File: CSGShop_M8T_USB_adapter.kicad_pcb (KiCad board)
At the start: 2 copper layers, 36.8 x 16.5 mm, 6 parts, among them J1 NEO-M8T Conn_02x06_Odd_Even, J2 Conn_01x05, J3 Conn_01x06_Male, J4 Conn_01x06_Male

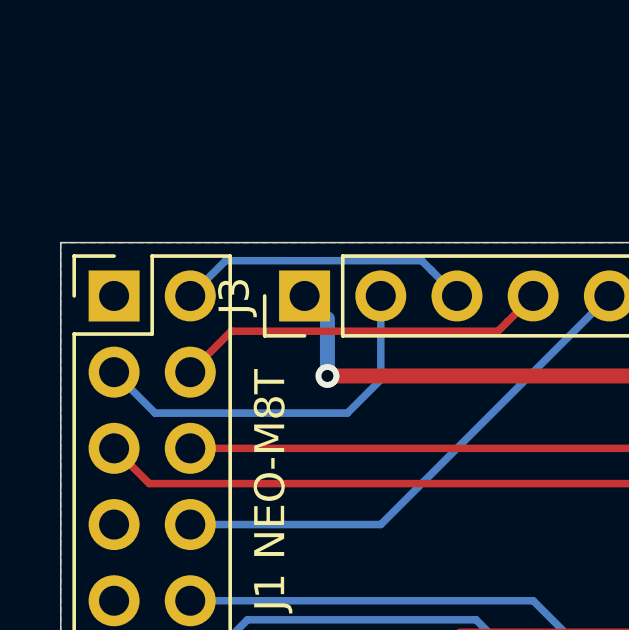
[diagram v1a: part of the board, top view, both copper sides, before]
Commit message: fix missing trace to GND on M8T header
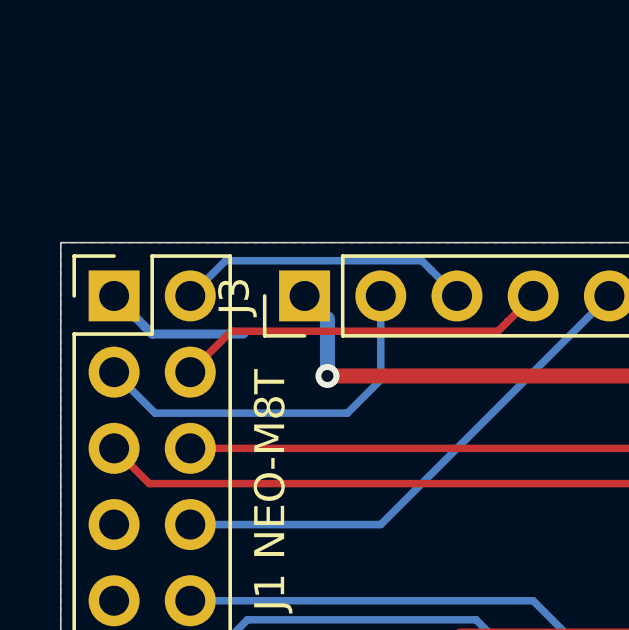
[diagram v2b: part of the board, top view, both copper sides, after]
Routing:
- net GND: track 55.3 -> 60.1 mm
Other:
- board text added: "CSGShop M8T (pin version) USB adapter V1.0.1"
- board text removed: "CSGShop M8T (pin version) USB adapter V1.0"
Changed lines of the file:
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@@
-(kicad_pcb (version 20171130) (host pcbnew 6.0.0-rc1-unknown-4d73cfb~66~ubuntu18.04.1)
+(kicad_pcb (version 20171130) (host pcbnew 6.0.0-rc1-unknown-ad07b4a~66~ubuntu18.04.1)
   (general
     (thickness 1.6)
     (drawings 12)
-    (tracks 46)
+    (tracks 49)
     (zones 0)
     (modules 6)
@@
   )
   (setup
-    (last_trace_width 0.25)
+    (last_trace_width 0.3)
+    (user_trace_width 0.3)
     (trace_clearance 0.2)
     (zone_clearance 0.508)
@@
     (effects (font (size 1 1) (thickness 0.15)) (justify mirror))
   )
-  (gr_text "CSGShop M8T \n(pin version) \nUSB adapter V1.0" (at 137.414 53.213) (layer B.SilkS)
+  (gr_text "CSGShop M8T \n(pin version) \nUSB adapter V1.0.1" (at 137.414 53.213) (layer B.SilkS)
     (effects (font (size 1 1) (thickness 0.15)) (justify mirror))
   )
@@
   (segment (start 132.08 48.26) (end 131.318 47.498) (width 0.25) (layer B.Cu) (net 1))
   (segment (start 132.08 50.165) (end 132.08 48.26) (width 0.5) (layer B.Cu) (net 1))
+  (segment (start 124.968 47.498) (end 125.984 48.514) (width 0.3) (layer B.Cu) (net 1))
+  (segment (start 125.984 48.514) (end 126.238 48.768) (width 0.3) (layer B.Cu) (net 1))
+  (segment (start 126.238 48.768) (end 129.286 48.768) (width 0.3) (layer B.Cu) (net 1))
   (segment (start 148.375001 56.046001) (end 149.225 56.896) (width 0.25) (layer F.Cu) (net 2))
   (segment (start 146.082001 53.753001) (end 148.375001 56.046001) (width 0.25) (layer F.Cu) (net 2))

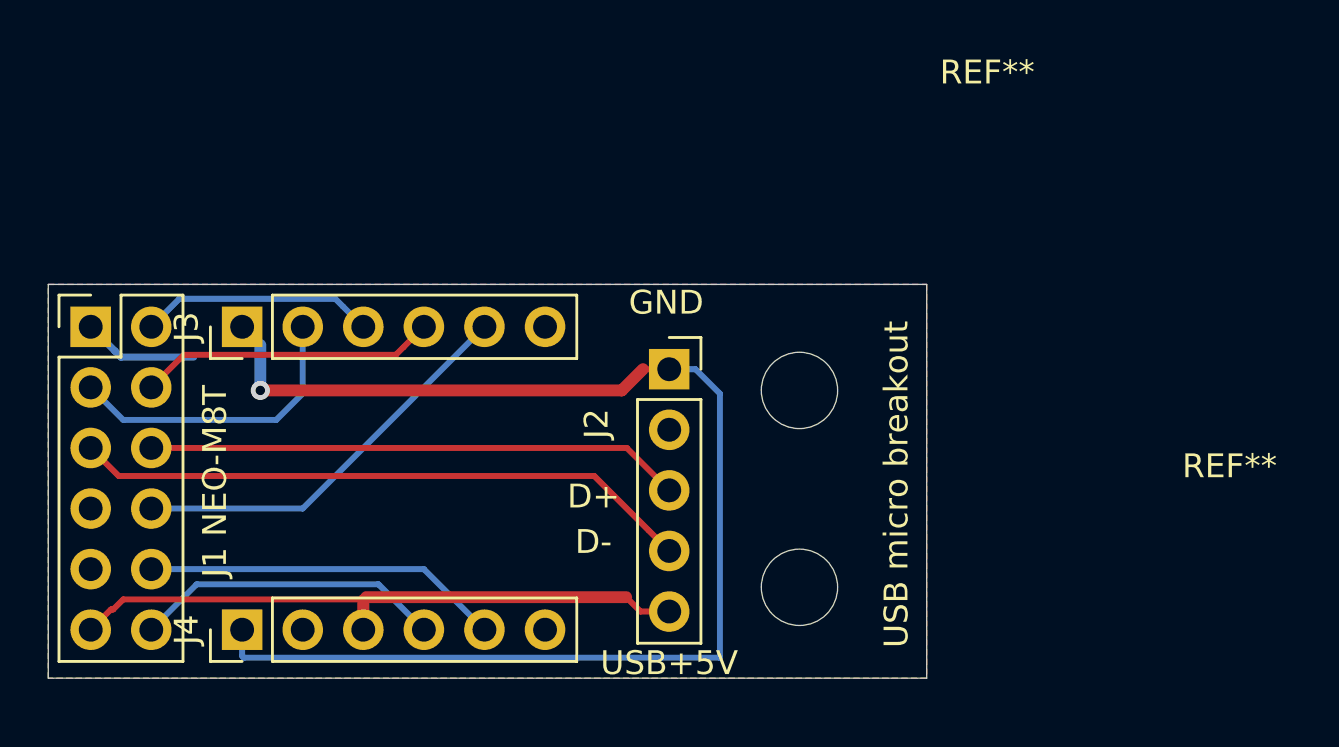
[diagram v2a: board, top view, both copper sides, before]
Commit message: add extra info on silk screen
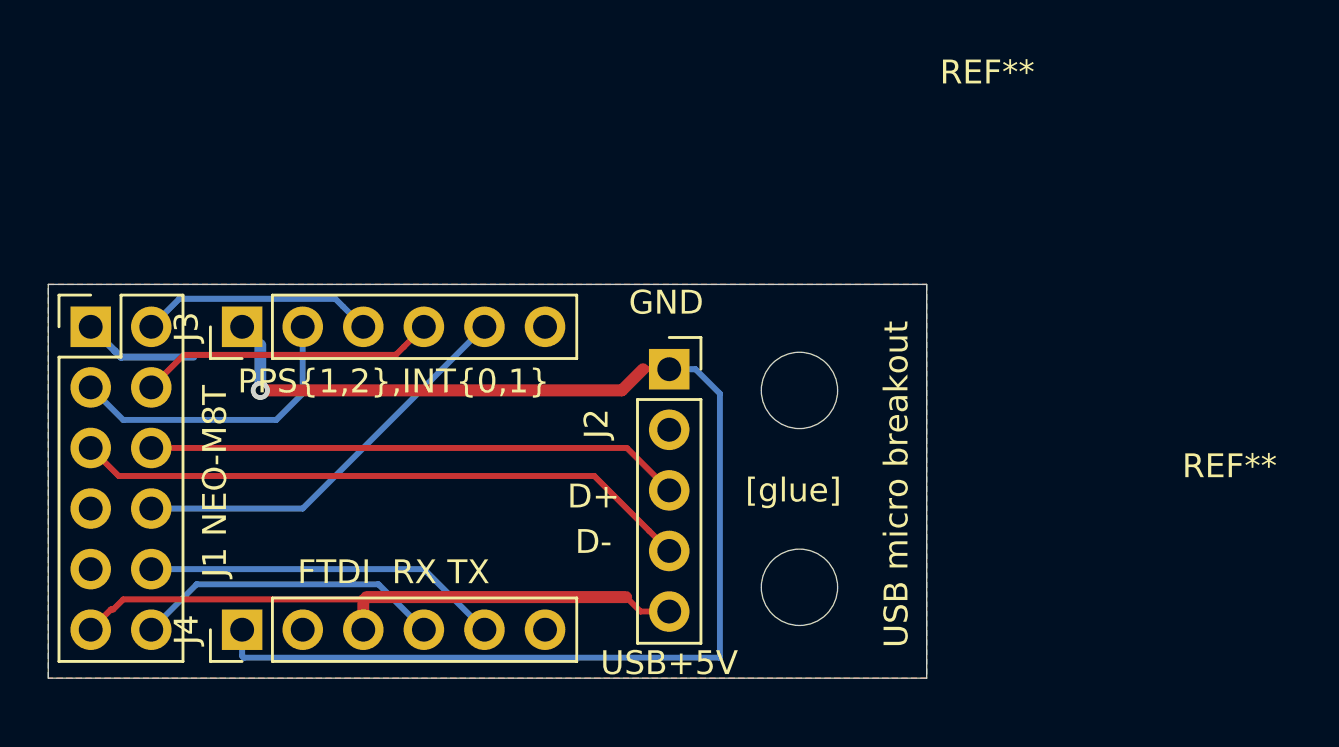
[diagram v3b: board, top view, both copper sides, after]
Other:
- board text added: "FTDI RX TX"
- board text added: "PPS{1,2},INT{0,1}"
- board text added: "[glue]"
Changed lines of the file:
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@@
   (general
     (thickness 1.6)
-    (drawings 12)
+    (drawings 15)
     (tracks 49)
     (zones 0)
@@
     (pad 1 np_thru_hole circle (at 0 0) (size 3.2 3.2) (drill 3.2) (layers *.Cu *.Mask))
   )
+  (gr_text [glue] (at 154.432 54.356) (layer F.SilkS)
+    (effects (font (size 1 1) (thickness 0.15)))
+  )
+  (gr_text PPS{1,2},INT{0,1} (at 137.668 49.784) (layer F.SilkS)
+    (effects (font (size 1 1) (thickness 0.15)))
+  )
+  (gr_text "FTDI  RX TX" (at 137.668 57.785) (layer F.SilkS)
+    (effects (font (size 1 1) (thickness 0.15)))
+  )
   (gr_text "USB micro breakout" (at 158.75 54.102 90) (layer F.SilkS)
